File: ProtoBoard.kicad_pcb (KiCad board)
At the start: 4 copper layers, 50 x 35 mm, 53 parts, among them IC1 L9110S, IC2 L9110S, IC3 L9110S, J1 Conn_01x02_Female, J11 Conn_01x10_Female, J2 Conn_01x08_Female, J3 I2C_STANDARDQWIIC, J4 Conn_01x10_Female, J5 Conn_01x05_Female, J6 Conn_01x05_Female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

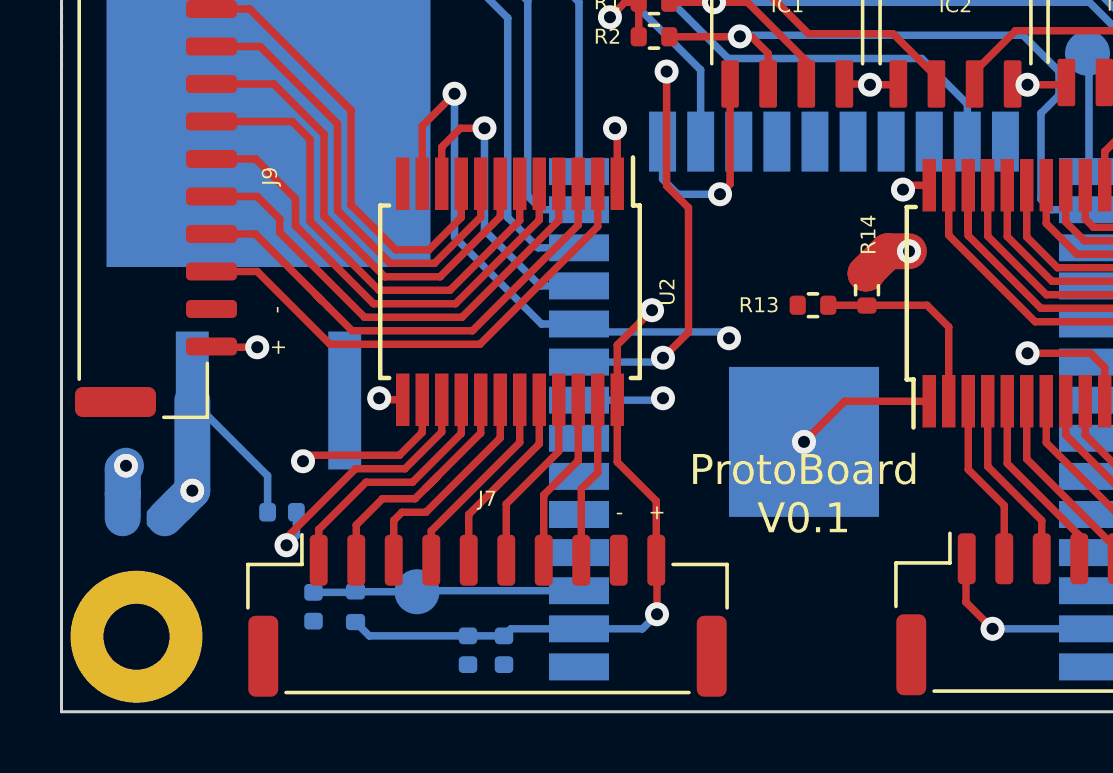
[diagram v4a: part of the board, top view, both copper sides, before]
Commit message: Remove diode
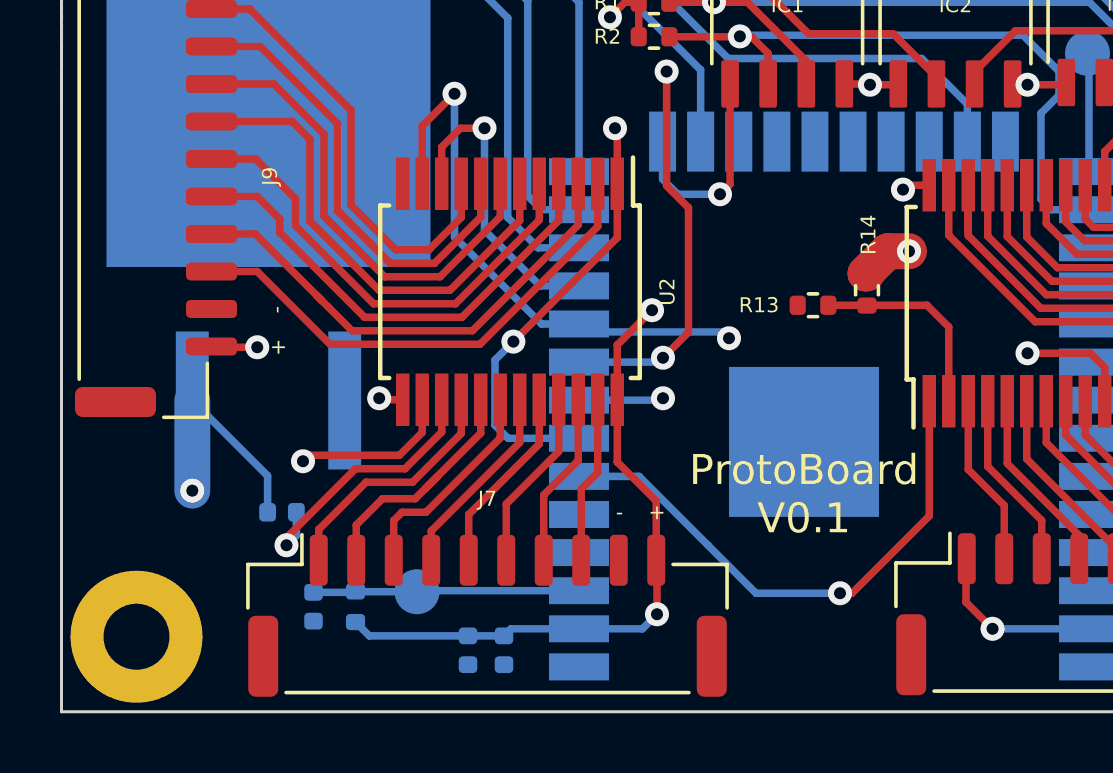
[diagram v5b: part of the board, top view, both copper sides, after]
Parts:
- removed D2: D, Diode_SMD:D_0402_1005Metric
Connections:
- J1 pad 2: Net-(D2-Pad2) -> +BATT
- U1 pad 6: unconnected-(U1-Pad6) -> /COM2
- U1 pad 7: unconnected-(U1-Pad7) -> /COM1
- U2 pad 1: GND -> /COM1
- U4 pad 1: GND -> /COM2
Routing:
- net Net-(D2-Pad2): track 23.3 -> 0.00 mm, vias 1 -> 0
- net +BATT: track 67.9 -> 86.5 mm
- net /COM2: track 0.00 -> 18.2 mm, vias 0 -> 1
- net /COM1: track 0.00 -> 14.6 mm, vias 0 -> 2
- net GND: track 43.6 -> 36.9 mm, vias 8 -> 6
